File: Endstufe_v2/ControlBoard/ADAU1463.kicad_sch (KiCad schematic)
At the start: 29 parts, among them U7 ADAU1463WBCPZ300, U8 ZPLR135_T8, Y2 24.576Mhz

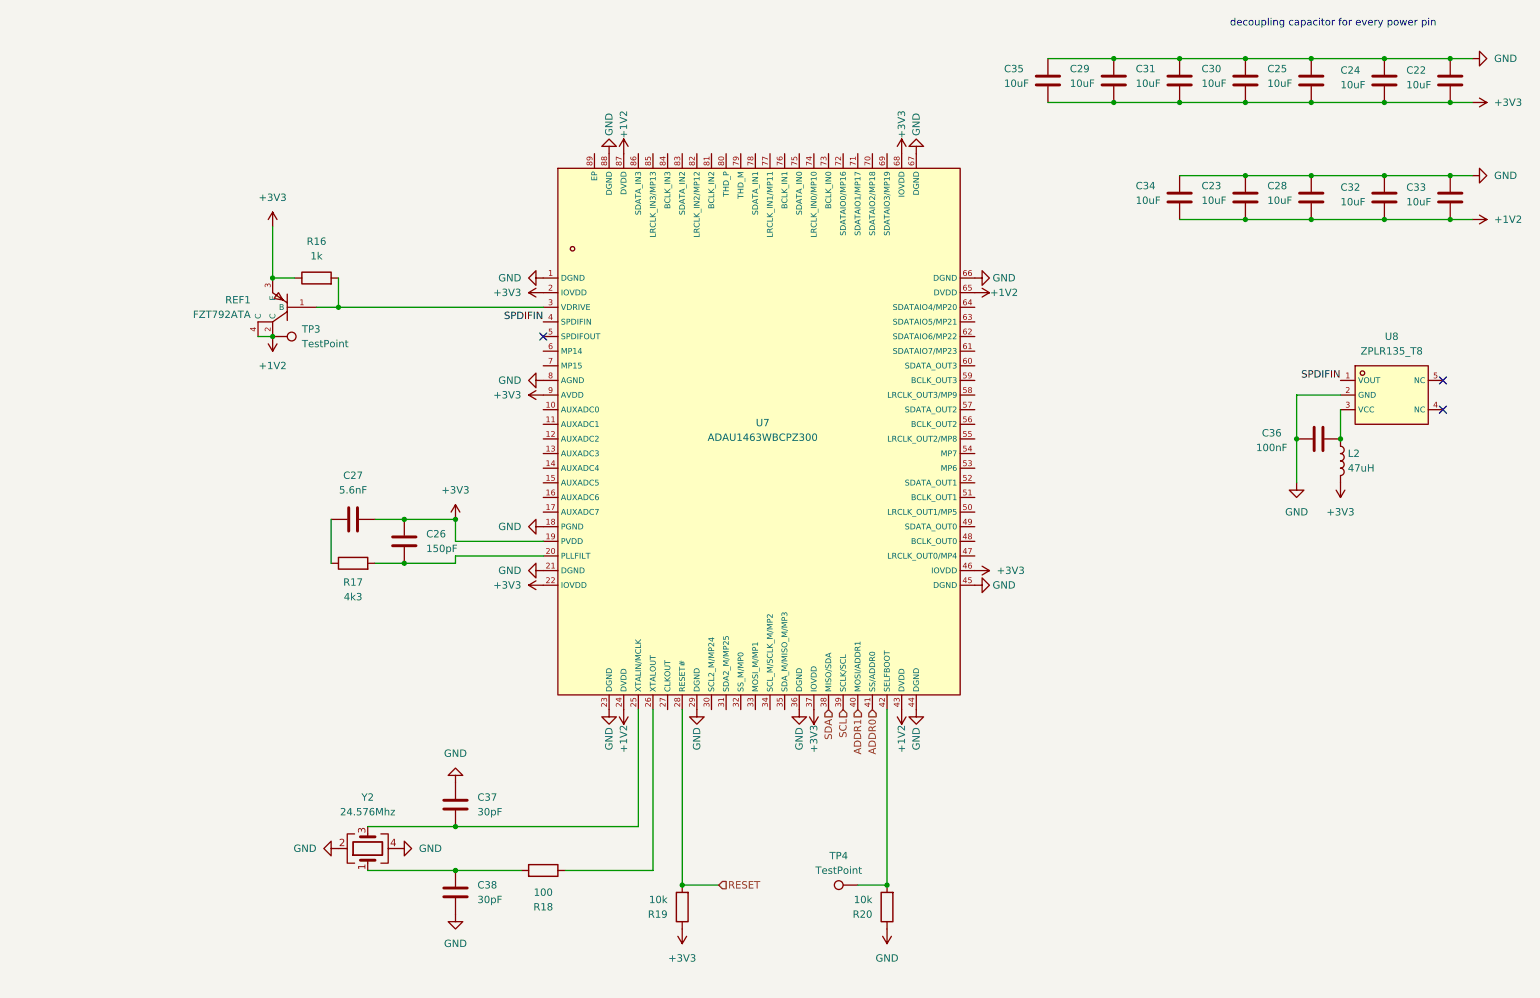
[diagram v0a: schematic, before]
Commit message: Fully connected ADAU1463
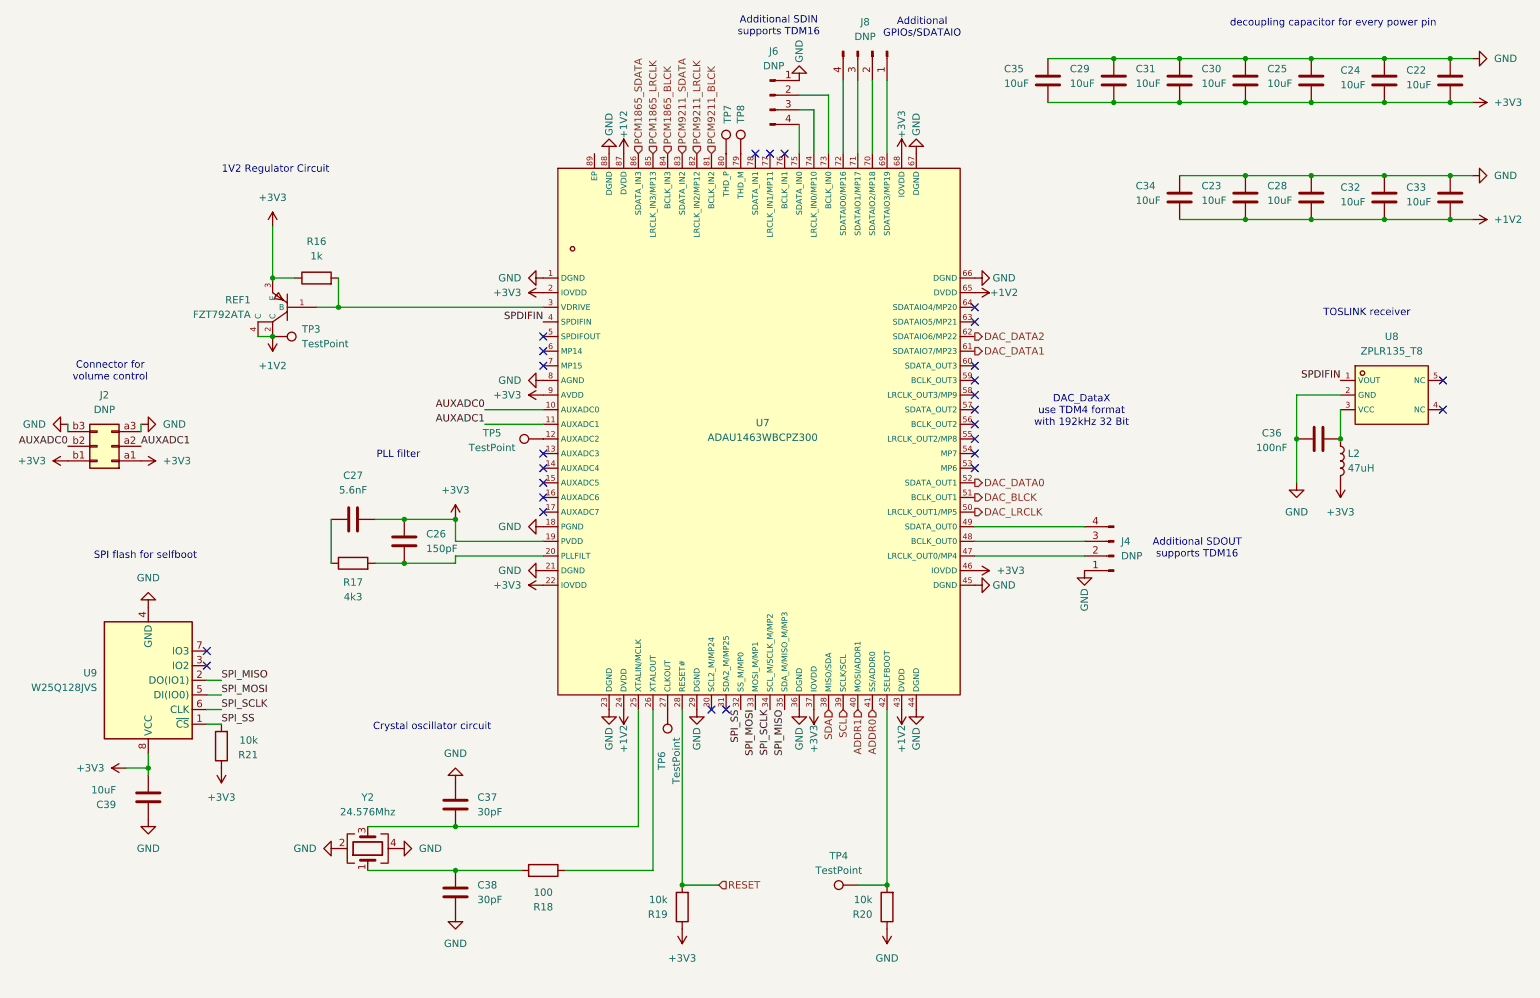
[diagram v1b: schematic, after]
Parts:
- added C39: 10uF, Endstufe:C_0402_1005Metric, symbol Endstufe:C
- added J2: DNP, symbol Connector_Generic:Conn_02x03_Row_Letter_First
- added J4, J6, J8: DNP, symbol Endstufe:Conn_01x04_Pin
- added R21: 10k, Endstufe:C_0402_1005Metric, symbol Endstufe:R
- added TP5, TP6, TP7, TP8: TestPoint, symbol Connector:TestPoint
- added U9: W25Q128JVS, Endstufe:SOIC-8_L5.3-W5.3-P1.27-LS8.0-BL, symbol Endstufe:W25Q128JVS
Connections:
- net +3V3: now also C39.2, J2.a1 (Pin_a1), J2.b1 (Pin_b1), R21.1, U9.8 (VCC)
- net GND: now also C39.1, J2.a3 (Pin_a3), J2.b3 (Pin_b3), J4.1 (Pin_1), J6.1 (Pin_1), U9.4 (GND)
- net AUXADC0: now reaches U7.10 (AUXADC0)
- net AUXADC0: now also J2.b2 (Pin_b2)
- net AUXADC1: now reaches U7.11 (AUXADC1)
- net AUXADC1: now also J2.a2 (Pin_a2)
- net at U7.12 (AUXADC2): now also TP5.1
- net at U7.27 (CLKOUT): now also TP6.1
- net SPI_SS: now reaches U7.32 (SS_M/MP0)
- net SPI_SS: now also R21.2, U9.1 (~{CS})
- net SPI_MOSI: now reaches U7.33 (MOSI_M/MP1)
- net SPI_MOSI: now also U9.5 (DI(IO0))
- net SPI_SCLK: now reaches U7.34 (SCL_M/SCLK_M/MP2)
- net SPI_SCLK: now also U9.6 (CLK)
- net SPI_MISO: now reaches U7.35 (SDA_M/MISO_M/MP3)
- net SPI_MISO: now also U9.2 (DO(IO1))
- net at U7.47 (LRCLK_OUT0/MP4): now also J4.2 (Pin_2)
- net at U7.48 (BCLK_OUT0): now also J4.3 (Pin_3)
- net at U7.49 (SDATA_OUT0): now also J4.4 (Pin_4)
- net DAC_LRCLK: now reaches U7.50 (LRCLK_OUT1/MP5)
- net DAC_BLCK: now reaches U7.51 (BCLK_OUT1)
- net DAC_DATA0: now reaches U7.52 (SDATA_OUT1)
- net DAC_DATA1: now reaches U7.61 (SDATAIO7/MP23)
- net DAC_DATA2: now reaches U7.62 (SDATAIO6/MP22)
- net at U7.69 (SDATAIO3/MP19): now also J8.1 (Pin_1)
- net at U7.70 (SDATAIO2/MP18): now also J8.2 (Pin_2)
- net at U7.71 (SDATAIO1/MP17): now also J8.3 (Pin_3)
- net at U7.72 (SDATAIO0/MP16): now also J8.4 (Pin_4)
- net at U7.73 (BCLK_IN0): now also J6.2 (Pin_2)
- net at U7.74 (LRCLK_IN0/MP10): now also J6.3 (Pin_3)
- net at U7.75 (SDATA_IN0): now also J6.4 (Pin_4)
- net at U7.79 (THD_M): now also TP8.1
- net at U7.80 (THD_P): now also TP7.1
- net PCM9211_BLCK: now reaches U7.81 (BCLK_IN2)
- net PCM9211_LRCLK: now reaches U7.82 (LRCLK_IN2/MP12)
- net PCM9211_SDATA: now reaches U7.83 (SDATA_IN2)
- net PCM1865_BLCK: now reaches U7.84 (BCLK_IN3)
- net PCM1865_LRCLK: now reaches U7.85 (LRCLK_IN3/MP13)
- net PCM1865_SDATA: now reaches U7.86 (SDATA_IN3)
- no-connect marks 3 -> 27
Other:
- note added: "1V2 Regulator Circuit"
- note added: "Additional GPIOs/SDATAIO"
- note added: "Additional SDIN supports TDM16"
- note added: "Additional SDOUT supports TDM16"
- note added: "Connector for volume control"
- note added: "Crystal oscillator circuit"
- note added: "DAC_DataX use TDM4 format with 192kHz 32 Bit"
- note added: "PLL filter"
- note added: "SPI flash for selfboot"
- note added: "TOSLINK receiver"

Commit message: Added ADAU1962A DAC schematic
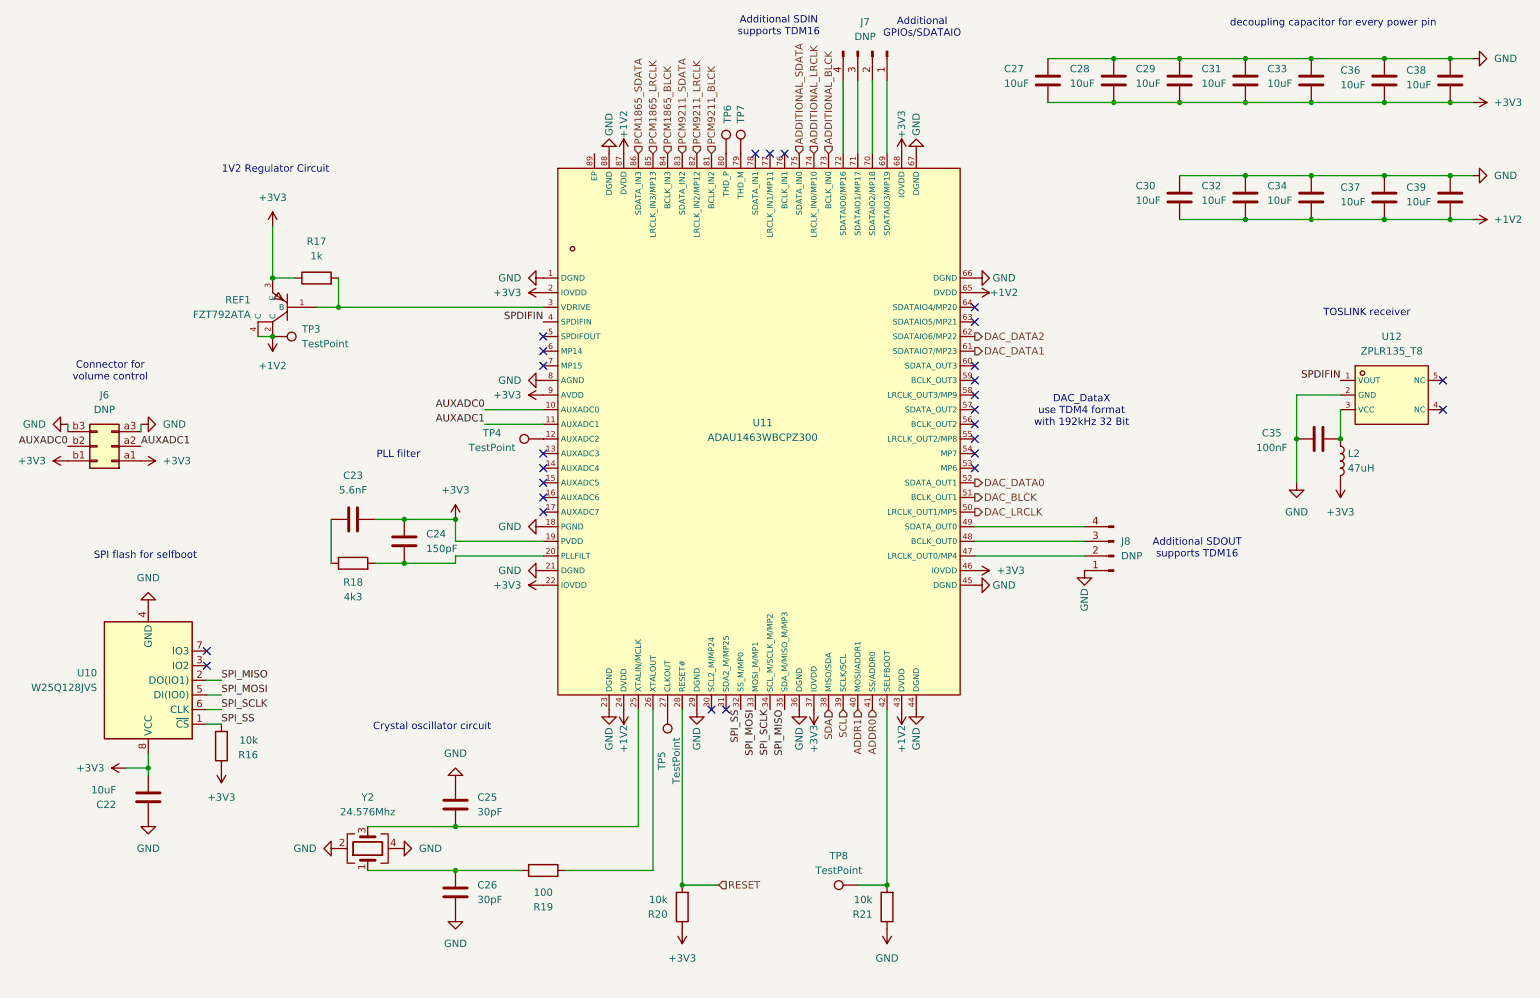
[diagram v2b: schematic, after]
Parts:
- removed J6: DNP, symbol Endstufe:Conn_01x04_Pin
- renumbered C39 to C22, C27 to C23, C26 to C24, C37 to C25, C38 to C26, C35 to C27, C29 to C28, C31 to C29, C34 to C30, C30 to C31, C23 to C32, C25 to C33, C28 to C34, C36 to C35, C24 to C36, C32 to C37, C22 to C38, C33 to C39, J2 to J6, J8 to J7, J4 to J8, R21 to R16, R16 to R17, R17 to R18, R18 to R19, R19 to R20, R20 to R21, TP5 to TP4, TP6 to TP5, TP7 to TP6, TP8 to TP7, TP4 to TP8, U9 to U10, U7 to U11, U8 to U12
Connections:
- net ADDITIONAL_BLCK: now reaches U11.73 (BCLK_IN0)
- net ADDITIONAL_LRCLK: now reaches U11.74 (LRCLK_IN0/MP10)
- net ADDITIONAL_SDATA: now reaches U11.75 (SDATA_IN0)

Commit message: Add footprints to all components
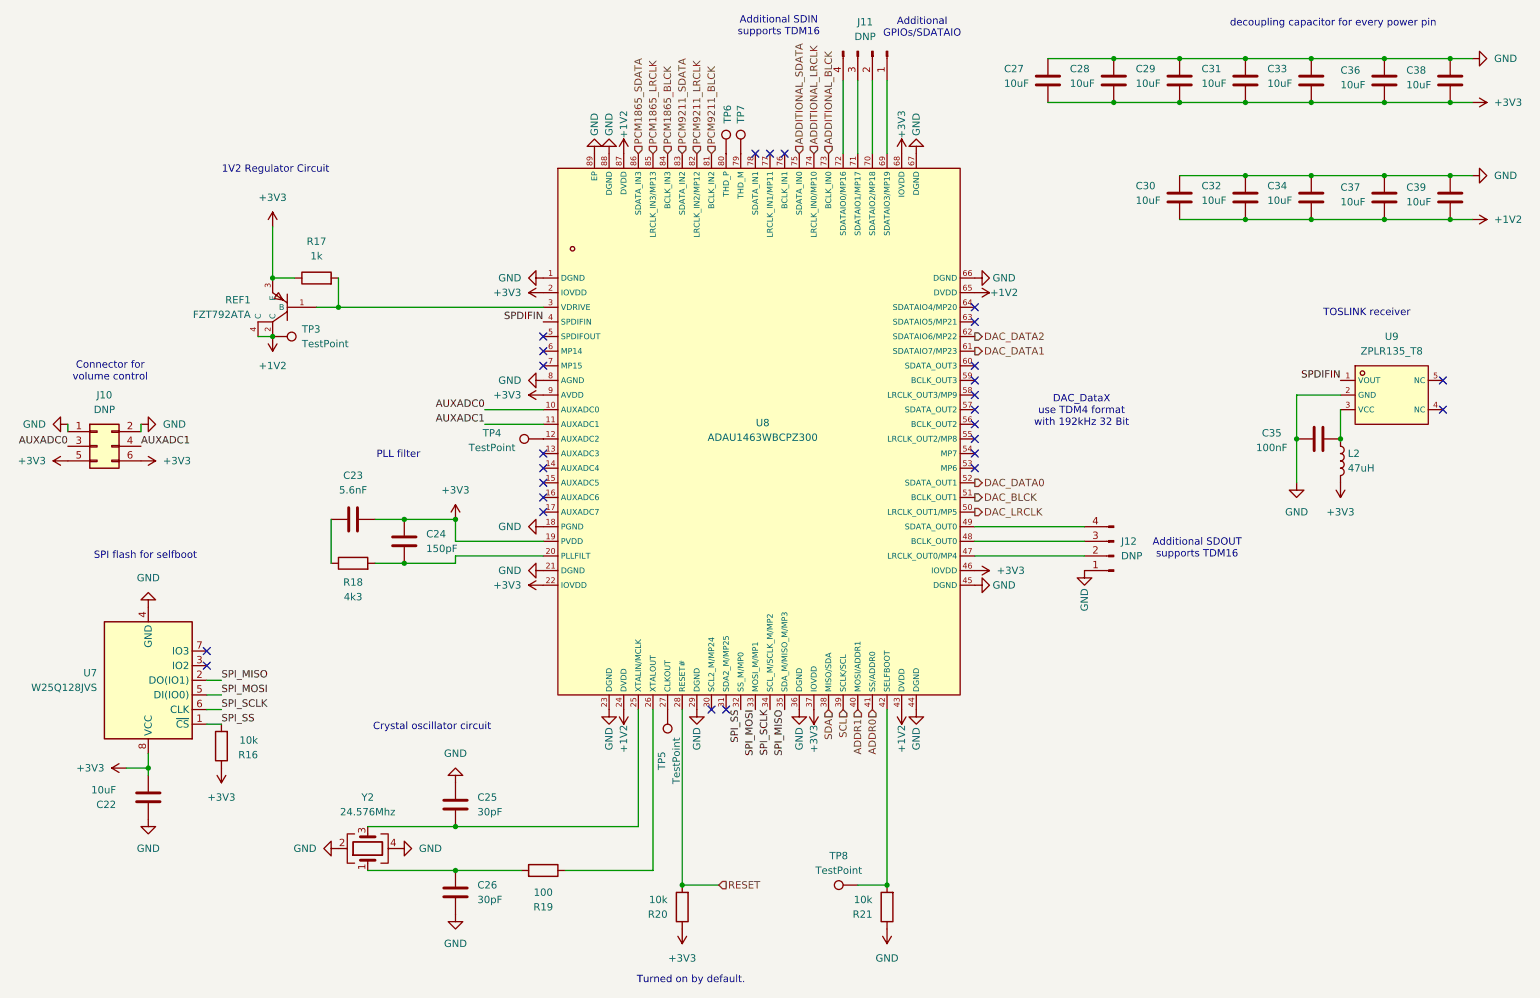
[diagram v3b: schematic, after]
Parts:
- J10: renamed from J6; footprint (none) -> Connector_PinHeader_2.54mm:PinHeader_2x03_P2.54mm_Vertical; symbol Connector_Generic:Conn_02x03_Row_Letter_First -> Connector_Generic:Conn_02x03_Odd_Even
- J11: renamed from J7; footprint (none) -> Connector_PinHeader_2.54mm:PinHeader_1x04_P2.54mm_Vertical
- J12: renamed from J8; footprint (none) -> Endstufe:CONN-TH_B4B-XH-2-LF-SN
- TP3, TP4, TP5, TP6, TP7, TP8: footprint (none) -> TestPoint:TestPoint_Pad_D1.0mm
- renumbered U10 to U7, U11 to U8, U12 to U9
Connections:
- net +3V3: now also J10.5 (Pin_5), J10.6 (Pin_6); no longer J10.a1 (Pin_a1), J10.b1 (Pin_b1)
- net AUXADC0: now also J10.3 (Pin_3); no longer J10.b2 (Pin_b2)
- net AUXADC1: now also J10.4 (Pin_4); no longer J10.a2 (Pin_a2)
- net GND: now also J10.1 (Pin_1), J10.2 (Pin_2), U8.89 (EP); no longer J10.a3 (Pin_a3), J10.b3 (Pin_b3)
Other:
- note added: "Turned on by default."
- moved on the sheet: J10
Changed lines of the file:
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@@
 		)
 	)
+	(text "Turned on by default.\n"
+		(exclude_from_sim no)
+		(at 134.874 190.5 0)
+		(effects
+			(font
+				(size 1.27 1.27)
+			)
+		)
+	)
 	(text "Additional SDOUT\nsupports TDM16"
 		(exclude_from_sim no)
@@
 			)
 		)
-		(property "Footprint" ""
+		(property "Footprint" "TestPoint:TestPoint_Pad_D1.0mm"
 			(at 146.05 46.99 0)
 			(effects
@@
 		(dnp no)
 		(fields_autoplaced yes)
-		(property "Reference" "J7"
+		(property "Reference" "J11"
 			(at 165.1 24.13 90)
 			(effects
@@
 			)
 		)
-		(property "Footprint" ""
+		(property "Footprint" "Connector_PinHeader_2.54mm:PinHeader_1x04_P2.54mm_Vertical"
 			(at 166.37 29.21 0)
 			(effects
@@
 			(project "ControlBoard"
 				(path "/4f887f51-77c1-41d4-a3eb-45d362caffe1/70b67e3d-1dd9-4820-9634-6ce668eb2a07"
-					(reference "J7")
+					(reference "J11")
 					(unit 1)
 				)
@@
 			)
 		)
-		(property "Footprint" ""
+		(property "Footprint" "TestPoint:TestPoint_Pad_D1.0mm"
 			(at 109.22 91.44 0)
 			(effects
@@
 			)
 		)
-		(property "Footprint" ""
+		(property "Footprint" "TestPoint:TestPoint_Pad_D1.0mm"
 			(at 148.59 46.99 0)
 			(effects
@@
 			)
 		)
-		(property "Footprint" ""
+		(property "Footprint" "TestPoint:TestPoint_Pad_D1.0mm"
 			(at 163.83 168.91 0)
 			(effects
@@
 		(dnp no)
 		(fields_autoplaced yes)
-		(property "Reference" "U12"
+		(property "Reference" "U9"
 			(at 256.54 78.74 0)
 			(effects
@@
 			(project "ControlBoard"
 				(path "/4f887f51-77c1-41d4-a3eb-45d362caffe1/70b67e3d-1dd9-4820-9634-6ce668eb2a07"
-					(reference "U12")
+					(reference "U9")
 					(unit 1)
 				)
@@
 		(dnp no)
 		(fields_autoplaced yes)
-		(property "Reference" "J8"
+		(property "Reference" "J12"
 			(at 209.55 114.2999 0)
 			(effects
@@
 			)
 		)
-		(property "Footprint" ""
+		(property "Footprint" "Endstufe:CONN-TH_B4B-XH-2-LF-SN"
 			(at 208.28 116.84 0)
 			(effects
@@
 			(project ""
 				(path "/4f887f51-77c1-41d4-a3eb-45d362caffe1/70b67e3d-1dd9-4820-9634-6ce668eb2a07"
-					(reference "J8")
+					(reference "J12")
 					(unit 1)
 				)
@@
 		(dnp no)
 		(fields_autoplaced yes)
-		(property "Reference" "U10"
+		(property "Reference" "U7"
 			(at 31.75 137.1599 0)
 			(effects
@@
 			(project "ControlBoard"
 				(path "/4f887f51-77c1-41d4-a3eb-45d362caffe1/70b67e3d-1dd9-4820-9634-6ce668eb2a07"
-					(reference "U10")
+					(reference "U7")
 					(unit 1)
 				)
@@
 	)
 	(symbol
+		(lib_id "Endstufe:GND")
+		(at 118.11 46.99 180)
+		(unit 1)
+		(exclude_from_sim no)
+		(in_bom yes)
+		(on_board yes)
+		(dnp no)
+		(property "Reference" "#PWR0137"
+			(at 118.11 40.64 0)
+			(effects
+				(font
+					(size 1.27 1.27)
+				)
+				(hide yes)
+			)
+		)
+		(property "Value" "GND"
+			(at 118.11 41.91 90)
+			(effects
+				(font
+					(size 1.27 1.27)
+				)
+			)
+		)
+		(property "Footprint" ""
+			(at 118.11 46.99 0)
+			(effects
+				(font
+					(size 1.27 1.27)
+				)
+				(hide yes)
+			)
+		)
+		(property "Datasheet" ""
+			(at 118.11 46.99 0)
+			(effects
+				(font
+					(size 1.27 1.27)
+				)
+				(hide yes)
+			)
+		)
+		(property "Description" "Power symbol creates a global label with name \"GND\" , ground"
+			(at 118.11 46.99 0)
+			(effects
+				(font
+					(size 1.27 1.27)
+				)
+				(hide yes)
+			)
+		)
+		(pin "1"
+		)
+		(instances
+			(project "ControlBoard"
+				(path "/4f887f51-77c1-41d4-a3eb-45d362caffe1/70b67e3d-1dd9-4820-9634-6ce668eb2a07"
+					(reference "#PWR0137")
+					(unit 1)
+				)
+			)
+		)
+	)
+	(symbol
 		(lib_id "Endstufe:C")
 		(at 242.57 54.61 0)
@@
 			)
 		)
-		(property "Footprint" ""
+		(property "Footprint" "TestPoint:TestPoint_Pad_D1.0mm"
 			(at 125.73 143.51 0)
 			(effects
@@
 			)
 		)
-		(property "Footprint" ""
+		(property "Footprint" "TestPoint:TestPoint_Pad_D1.0mm"
 			(at 62.23 83.82 0)
 			(effects
@@
 		(on_board yes)
 		(dnp no)
-		(property "Reference" "U11"
+		(property "Reference" "U8"
 			(at 147.32 93.726 0)
 			(effects
@@
 			(project "ControlBoard"
 				(path "/4f887f51-77c1-41d4-a3eb-45d362caffe1/70b67e3d-1dd9-4820-9634-6ce668eb2a07"
-					(reference "U11")
+					(reference "U8")
 					(unit 1)
 				)
@@
 	)
 	(symbol
-		(lib_id "Connector_Generic:Conn_02x03_Row_Letter_First")
-		(at 34.29 97.79 180)
+		(lib_id "Connector_Generic:Conn_02x03_Odd_Even")
+		(at 31.75 97.79 0)
 		(unit 1)
 		(exclude_from_sim no)
@@
 		(dnp no)
 		(fields_autoplaced yes)
-		(property "Reference" "J6"
+		(property "Reference" "J10"
 			(at 33.02 88.9 0)
 			(effects
@@
 			)
 		)
-		(property "Footprint" ""
-			(at 34.29 97.79 0)
+		(property "Footprint" "Connector_PinHeader_2.54mm:PinHeader_2x03_P2.54mm_Vertical"
+			(at 31.75 97.79 0)
 			(effects
 				(font
@@
 		)
 		(property "Datasheet" "~"
-			(at 34.29 97.79 0)
+			(at 31.75 97.79 0)
 			(effects
 				(font
@@
 			)
 		)
-		(property "Description" "Generic connector, double row, 02x03, row letter first pin numbering scheme (pin number consists of a letter for the row and a number for the pin index in this row. a1, ..., aN; b1, ..., bN), script generated (kicad-library-utils/schlib/autogen/connector/)"
-			(at 34.29 97.79 0)
+		(property "Description" "Generic connector, double row, 02x03, odd/even pin numbering scheme (row 1 odd numbers, row 2 even numbers), script generated (kicad-library-utils/schlib/autogen/connector/)"
+			(at 31.75 97.79 0)
 			(effects
 				(font
@@
 			)
 		)
-		(pin "b2"
+		(pin "6"
 		)
-		(pin "b3"
+		(pin "4"
 		)
-		(pin "a2"
+		(pin "3"
 		)
-		(pin "a1"
+		(pin "1"
 		)
-		(pin "b1"
+		(pin "5"
 		)
-		(pin "a3"
+		(pin "2"
 		)
 		(instances
 			(project ""
 				(path "/4f887f51-77c1-41d4-a3eb-45d362caffe1/70b67e3d-1dd9-4820-9634-6ce668eb2a07"
-					(reference "J6")
+					(reference "J10")
 					(unit 1)
 				)
